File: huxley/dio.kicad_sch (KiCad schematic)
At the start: 1 part

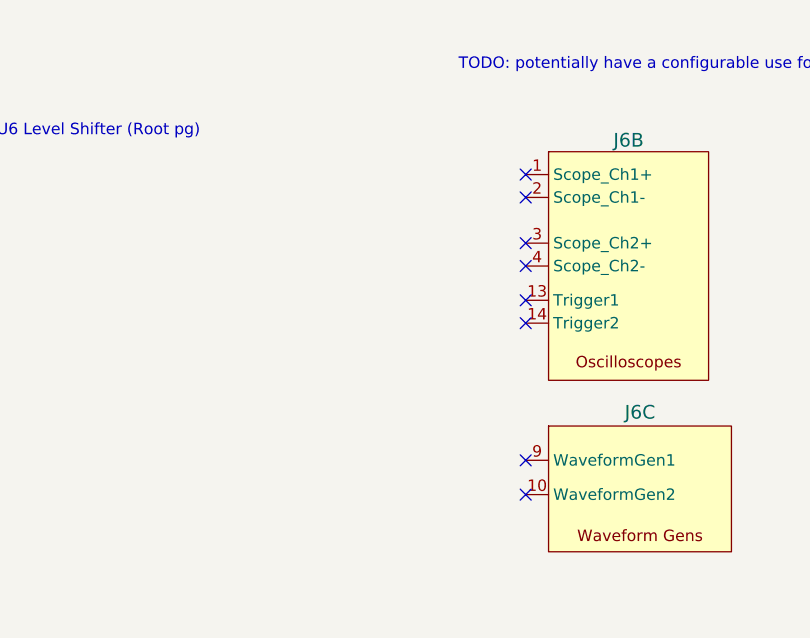
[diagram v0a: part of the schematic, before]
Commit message: removed all via-in-pad; added CLK connection to analogdiscovery signal generator
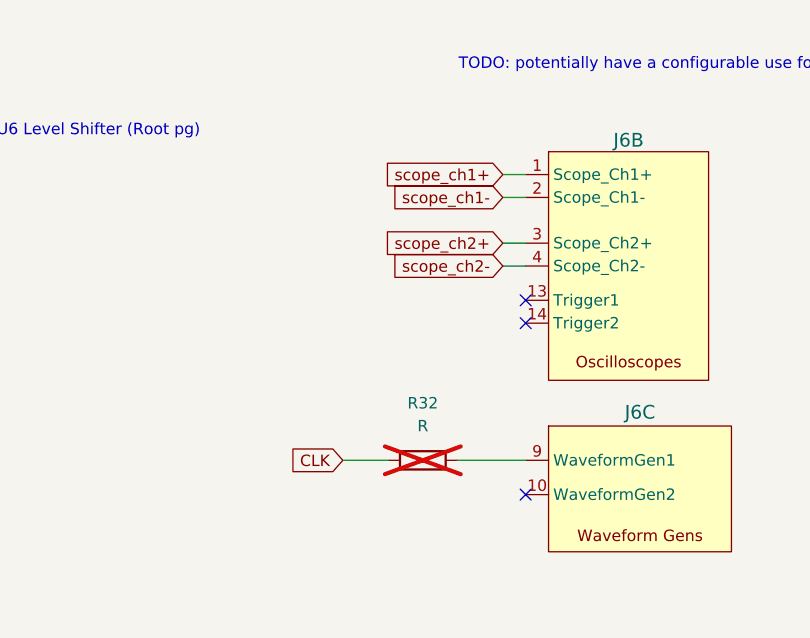
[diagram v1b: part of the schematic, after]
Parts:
- added R32: R, Resistor_SMD:R_0603_1608Metric, symbol Device:R
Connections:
- net scope_ch1+: now reaches J6.1 (Scope_Ch1+)
- net scope_ch1-: now reaches J6.2 (Scope_Ch1-)
- net scope_ch2+: now reaches J6.3 (Scope_Ch2+)
- net scope_ch2-: now reaches J6.4 (Scope_Ch2-)
- net at J6.9 (WaveformGen1): now also R32.2
- new net CLK: R32.1
- no-connect marks 11 -> 6
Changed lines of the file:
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@@
-	)
-	(no_connect
-		(at 180.34 68.58)
 	)
 	(no_connect
@@
 	)
 	(no_connect
-		(at 180.34 73.66)
-	)
-	(no_connect
 		(at 180.34 82.55)
 	)
@@
 		(at 78.74 82.55)
 	)
-	(no_connect
-		(at 180.34 76.2)
-	)
-	(no_connect
-		(at 180.34 66.04)
-	)
-	(no_connect
-		(at 180.34 97.79)
-	)
 	(wire
 		(pts
@@
 	(wire
 		(pts
+			(xy 160.02 97.79) (xy 165.1 97.79)
+		)
+		(stroke
+			(width 0)
+			(type default)
+		)
+	)
+	(wire
+		(pts
 			(xy 77.47 134.62) (xy 77.47 137.16)
 		)
@@
 	(wire
 		(pts
+			(xy 177.8 68.58) (xy 180.34 68.58)
+		)
+		(stroke
+			(width 0)
+			(type default)
+		)
+	)
+	(wire
+		(pts
 			(xy 76.2 64.77) (xy 78.74 64.77)
 		)
@@
 	(wire
 		(pts
+			(xy 177.8 66.04) (xy 180.34 66.04)
+		)
+		(stroke
+			(width 0)
+			(type default)
+		)
+	)
+	(wire
+		(pts
 			(xy 77.47 129.54) (xy 77.47 132.08)
 		)
@@
 	(wire
 		(pts
+			(xy 177.8 73.66) (xy 180.34 73.66)
+		)
+		(stroke
+			(width 0)
+			(type default)
+		)
+	)
+	(wire
+		(pts
 			(xy 76.2 77.47) (xy 78.74 77.47)
 		)
@@
 	(wire
 		(pts
+			(xy 177.8 76.2) (xy 180.34 76.2)
+		)
+		(stroke
+			(width 0)
+			(type default)
+		)
+	)
+	(wire
+		(pts
 			(xy 101.6 74.93) (xy 99.06 74.93)
 		)
@@
 		(pts
 			(xy 101.6 77.47) (xy 99.06 77.47)
+		)
+		(stroke
+			(width 0)
+			(type default)
+		)
+	)
+	(wire
+		(pts
+			(xy 172.72 97.79) (xy 180.34 97.79)
 		)
 		(stroke
@@
 		)
 	)
+	(global_label "CLK"
+		(shape input)
+		(at 160.02 97.79 180)
+		(fields_autoplaced yes)
+		(effects
+			(font
+				(size 1.27 1.27)
+			)
+			(justify right)
+		)
+		(property "Intersheetrefs" "${INTERSHEET_REFS}"
+			(at 153.4667 97.79 0)
+			(effects
+				(font
+					(size 1.27 1.27)
+				)
+				(justify right)
+				(hide yes)
+			)
+		)
+	)
+	(global_label "scope_ch1+"
+		(shape input)
+		(at 177.8 66.04 180)
+		(fields_autoplaced yes)
+		(effects
+			(font
+				(size 1.27 1.27)
+			)
+			(justify right)
+		)
+		(property "Intersheetrefs" "${INTERSHEET_REFS}"
+			(at 163.3244 66.04 0)
+			(effects
+				(font
+					(size 1.27 1.27)
+				)
+				(justify right)
+				(hide yes)
+			)
+		)
+	)
 	(global_label "IBIAS_SEL2"
 		(shape output)
@@
 		)
 	)
+	(global_label "scope_ch1-"
+		(shape input)
+		(at 177.8 68.58 180)
+		(fields_autoplaced yes)
+		(effects
+			(font
+				(size 1.27 1.27)
+			)
+			(justify right)
+		)
+		(property "Intersheetrefs" "${INTERSHEET_REFS}"
+			(at 163.3244 68.58 0)
+			(effects
+				(font
+					(size 1.27 1.27)
+				)
+				(justify right)
+				(hide yes)
+			)
+		)
+	)
 	(global_label "IBIAS_SEL3"
 		(shape output)
@@
 		(property "Intersheetrefs" "${INTERSHEET_REFS}"
 			(at 62.8734 77.47 0)
+			(effects
+				(font
+					(size 1.27 1.27)
+				)
+				(justify right)
+				(hide yes)
+			)
+		)
+	)
+	(global_label "scope_ch2+"
+		(shape input)
+		(at 177.8 73.66 180)
+		(fields_autoplaced yes)
+		(effects
+			(font
+				(size 1.27 1.27)
+			)
+			(justify right)
+		)
+		(property "Intersheetrefs" "${INTERSHEET_REFS}"
+			(at 163.3244 73.66 0)
+			(effects
+				(font
+					(size 1.27 1.27)
+				)
+				(justify right)
+				(hide yes)
+			)
+		)
+	)
+	(global_label "scope_ch2-"
+		(shape input)
+		(at 177.8 76.2 180)
+		(fields_autoplaced yes)
+		(effects
+			(font
+				(size 1.27 1.27)
+			)
+			(justify right)
+		)
+		(property "Intersheetrefs" "${INTERSHEET_REFS}"
+			(at 163.3244 76.2 0)
 			(effects
 				(font
@@
 					(unit 1)
 				)
+			)
+		)
+	)
+	(symbol
+		(lib_id "Device:R")
+		(at 168.91 97.79 90)
+		(unit 1)
+		(exclude_from_sim no)
+		(in_bom yes)
+		(on_board yes)
+		(dnp yes)
+		(fields_autoplaced yes)
+		(property "Reference" "R32"
+			(at 168.91 91.44 90)
+			(effects
+				(font
+					(size 1.27 1.27)
+				)
+			)
+		)
+		(property "Value" "R"
+			(at 168.91 93.98 90)
+			(effects
+				(font
+					(size 1.27 1.27)
+				)
+			)
+		)
+		(property "Footprint" "Resistor_SMD:R_0603_1608Metric"
+			(at 168.91 99.568 90)
+			(effects
+				(font
+					(size 1.27 1.27)
+				)
+				(hide yes)
+			)
+		)
+		(property "Datasheet" "~"
+			(at 168.91 97.79 0)
+			(effects
+				(font
+					(size 1.27 1.27)
+				)
+				(hide yes)
+			)
+		)
+		(property "Description" "Resistor"
+			(at 168.91 97.79 0)
+			(effects
+				(font
+					(size 1.27 1.27)
+				)
+				(hide yes)
+			)
+		)
+		(pin "2"
+		)
+		(pin "1"
+		)
+		(instances
+			(project "huxley"
+				(path "/c6103430-c27a-4e90-8e2e-9404255f5ee3/7cec0b79-e39e-4de3-8e85-24df4d89a11b"
+					(reference "R32")
+					(unit 1)
+				)
